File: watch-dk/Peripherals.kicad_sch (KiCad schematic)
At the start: 46 parts, among them IC501 APDS-9306-065, IC502 BMI270, IC503 LIS2MDLTR, IC504 BMP581, IC505 DRV2603RUNT, IC506 PCA9306JK, IC507 RV-8263-C8, J501 Jumper, J502 Jumper, J503 Jumper, J504 Jumper, J505 Jumper, J506 Jumper, J507 Jumper, M501 Vibrator DC Motor, Q501 PMZB320UPEYL, X501 Current, X502 I2S, X503 Current, X504 I2C, X505 Current, X506 Current, X507 Current, X508 Current, X509 Motor, X510 Current

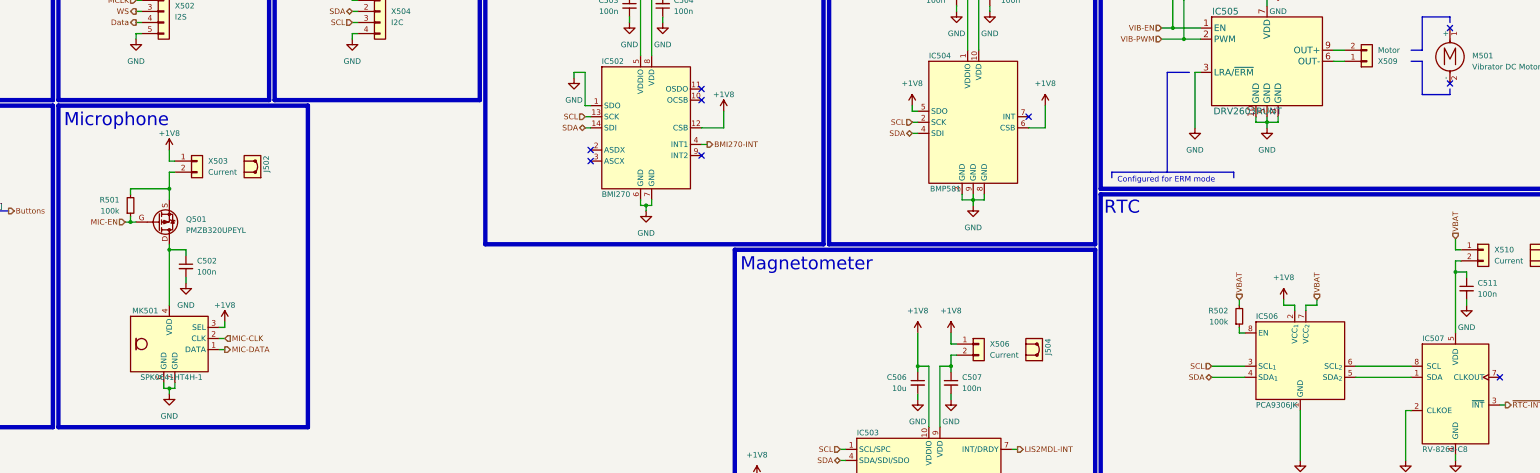
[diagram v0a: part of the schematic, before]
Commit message: Feature: Issue #145
- Update symbols

Signed-off-by: Daniel Kampert <DanielKampert@kampis-elektroecke.de>
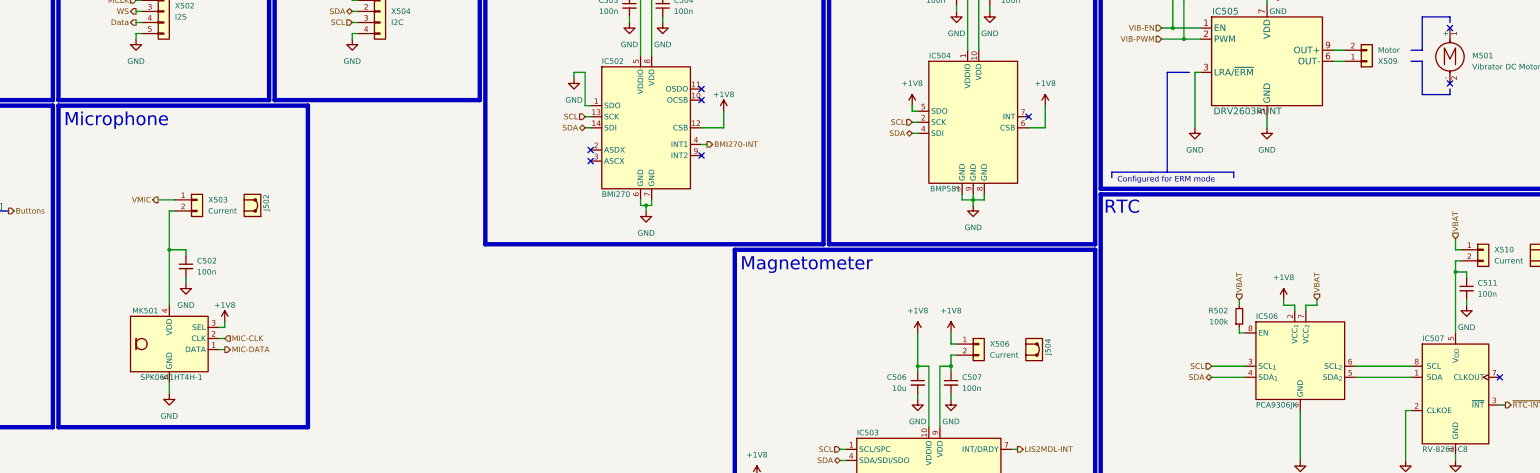
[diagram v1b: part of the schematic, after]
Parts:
- removed Q501: PMZB320UPEYL, Package_DFN_Kampi:DFN-1006-3, symbol Nexperia:PMZB320UPE
- removed R501: 100k, Resistor_SMD:R_0402_1005Metric, symbol Device:R_Small
- IC501: footprint Broadcom:Broadcom_DFN-6_2x2mm_P0.65mm -> OptoDevice:Broadcom_DFN-6_2x2mm_P0.65mm
- IC505: symbol TexasInstruments_Kampi:DRV2603RUNT -> Texas Instruments:DRV2603RUNT
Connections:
- net +1V8: no longer X503.1 (Pin_1)
- net at C502.1, MK501.4 (VDD): now also X503.2 (Pin_2)
- new net VMIC: X503.1 (Pin_1)
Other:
- moved on the sheet: J502, X503

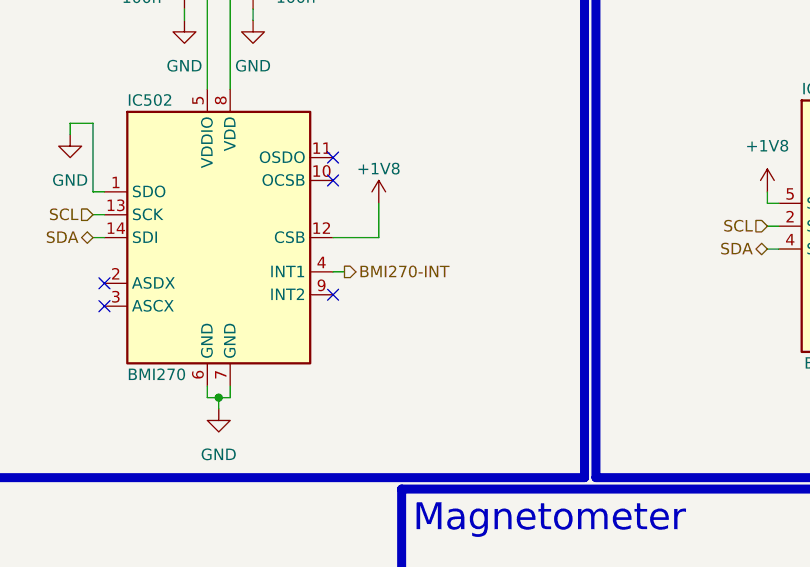
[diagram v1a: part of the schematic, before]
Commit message: Bug: Issue #146
Signed-off-by: Daniel Kampert <DanielKampert@kampis-elektroecke.de>
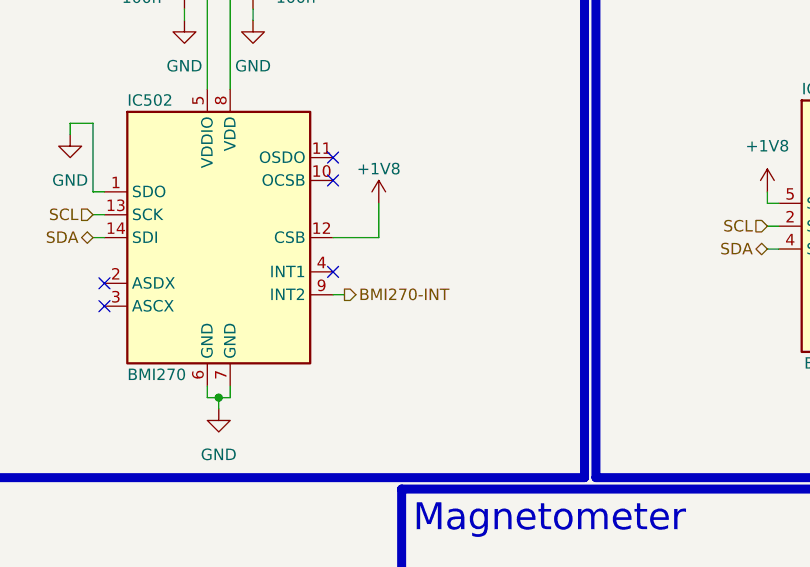
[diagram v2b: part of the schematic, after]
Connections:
- net BMI270-INT: now also IC502.9 (INT2); no longer IC502.4 (INT1)
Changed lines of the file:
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@@
 	)
 	(no_connect
-		(at 208.28 83.82)
+		(at 208.28 81.28)
 	)
 	(no_connect
@@
 		)
 	)
-	(wire
-		(pts
-			(xy 209.55 81.28) (xy 208.28 81.28)
-		)
-		(stroke
-			(width 0)
-			(type default)
-		)
-	)
 	(polyline
 		(pts
@@
 		(pts
 			(xy 240.03 153.67) (xy 241.3 153.67)
+		)
+		(stroke
+			(width 0)
+			(type default)
+		)
+	)
+	(wire
+		(pts
+			(xy 208.28 83.82) (xy 209.55 83.82)
 		)
 		(stroke
@@
 	(hierarchical_label "BMI270-INT"
 		(shape output)
-		(at 209.55 81.28 0)
+		(at 209.55 83.82 0)
 		(effects
 			(font

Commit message: Feature: Issue #149
Signed-off-by: Daniel Kampert <DanielKampert@kampis-elektroecke.de>
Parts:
- added TP503: MIC-CLK, TestPoint:TestPoint_Pad_D1.0mm, symbol Connector:TestPoint
- added TP504: MIC-Data, TestPoint:TestPoint_Pad_D1.0mm, symbol Connector:TestPoint
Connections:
- net MIC-CLK: now also TP503.1
- net MIC-DATA: now also TP504.1
